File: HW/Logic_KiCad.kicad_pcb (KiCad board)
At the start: 2 copper layers, 100 x 100 mm, 248 parts, among them J1 USB_B_Micro, Q1 Q_NPN_BEC, Q2 Q_NPN_BEC, Q4 Q_NMOS_SDG, Q5 Q_PMOS_SDG, Q6 Q_NMOS_SDG, Q7 Q_PMOS_SDG, Q8 Q_NMOS_SDG, Q9 Q_PMOS_SDG, SW1 SW_SPDT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

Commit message: routing PCB
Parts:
- moved D7 2.34 mm to (107.0, 48.5)
- moved D8 1.84 mm to (107.0, 50.6)
- moved C22 1.57 mm to (107.0, 66.4)
- moved C23 1.56 mm to (105.9, 66.4)
- moved Q1 0.62 mm to (98.4, 72.5)
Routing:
- net GND: track 0.00 -> 515.8 mm, vias 0 -> 119
- net V_LED_1: track 0.00 -> 300.2 mm, vias 0 -> 37
- net V_LED_3: track 0.00 -> 205.2 mm, vias 0 -> 25
- net V_LED_2: track 0.00 -> 197.8 mm, vias 0 -> 25
- net BTN_ENTER: track 0.00 -> 119.6 mm, vias 0 -> 2
- net BTN_NEW_GAME: track 0.00 -> 97.0 mm, vias 0 -> 2
- net BARVA_5: track 0.00 -> 92.9 mm, vias 0 -> 2
- net DATA_hodnoceni_LED: track 0.00 -> 88.8 mm, vias 0 -> 2
- net BARVA_4: track 0.00 -> 88.8 mm, vias 0 -> 2
- net +5V: track 0.00 -> 87.1 mm, vias 0 -> 4
- net BARVA_6: track 0.00 -> 82.6 mm, vias 0 -> 2
- net ZAPINANI_1_CAST_LED: track 0.00 -> 72.0 mm, vias 0 -> 2
- net BARVA_3: track 0.00 -> 61.2 mm
- net DATA_herni_LED: track 0.00 -> 56.6 mm, vias 0 -> 2
- net DATA_zadani_LED: track 0.00 -> 56.5 mm, vias 0 -> 2
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- added copper zone on In1.Cu, net +3V3
- added copper zone on In1.Cu, net +5V
- added copper zone on In2.Cu, net GND
- added copper zone on In1.Cu, net V_LED_1
- added copper zone on In1.Cu, net V_LED_2
- added copper zone on In1.Cu, net V_LED_3
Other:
- copper layers 2 -> 4

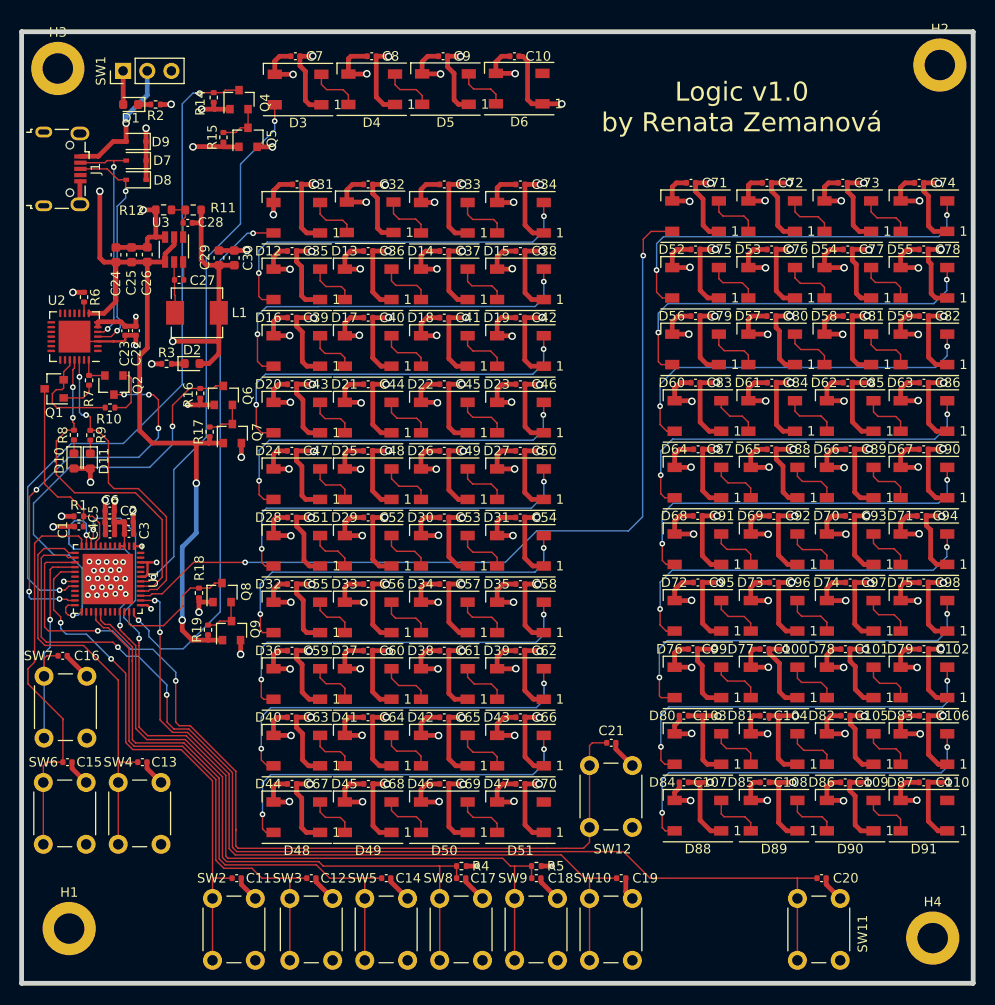
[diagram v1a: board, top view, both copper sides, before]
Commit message: add rounded corners PCB, place mounting holes
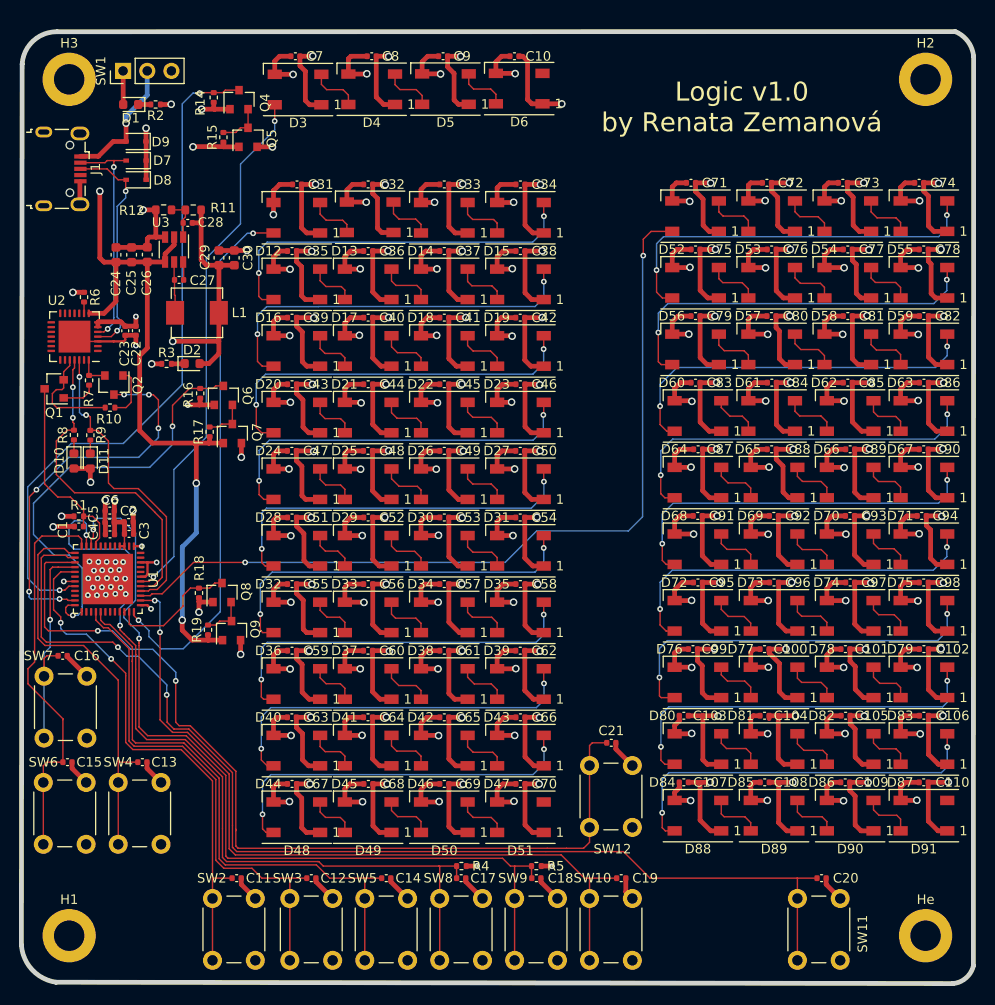
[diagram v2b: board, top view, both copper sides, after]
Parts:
- moved H2 2.12 mm to (190.0, 40.0)
- moved H3 1.65 mm to (100.0, 40.0)
- moved He 0.79 mm to (190.0, 130.0)
- moved H1 0.75 mm to (100.0, 130.0)
- renumbered H4 to He
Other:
- board size 100 x 100 mm -> 100.1 x 100 mm
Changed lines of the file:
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@@
   (general
     (thickness 1.6)
-    (drawings 6)
+    (drawings 10)
     (tracks 2381)
     (zones 0)
@@
     (mod_text_size 1 1)
     (mod_text_width 0.15)
-    (pad_size 1.524 1.524)
-    (pad_drill 0.762)
+    (pad_size 5.6 5.6)
+    (pad_drill 3.2)
     (pad_to_mask_clearance 0.05)
     (aux_axis_origin 0 0)
@@
   )
   (module MountingHole:MountingHole_3.2mm_M3_DIN965_Pad (layer F.Cu)
-    (at 190.75 130.25)
+    (at 190 130)
     (descr "Mounting Hole 3.2mm, M3, DIN965")
     (tags "mounting hole 3.2mm m3 din965")
     (attr virtual)
-    (fp_text reference H4 (at 0 -3.8) (layer F.SilkS)
+    (fp_text reference He (at 0 -3.8) (layer F.SilkS)
       (effects (font (size 1 1) (thickness 0.15)))
     )
@@
   )
   (module MountingHole:MountingHole_3.2mm_M3_DIN965_Pad (layer F.Cu)
-    (at 98.806 38.862)
+    (at 100 40)
     (descr "Mounting Hole 3.2mm, M3, DIN965")
     (tags "mounting hole 3.2mm m3 din965")
@@
   )
   (module MountingHole:MountingHole_3.2mm_M3_DIN965_Pad (layer F.Cu)
-    (at 191.5 38.5)
+    (at 190 40)
     (descr "Mounting Hole 3.2mm, M3, DIN965")
     (tags "mounting hole 3.2mm m3 din965")
@@
   )
   (module MountingHole:MountingHole_3.2mm_M3_DIN965_Pad (layer F.Cu)
-    (at 100 129.25)
+    (at 100 130)
     (descr "Mounting Hole 3.2mm, M3, DIN965")
     (tags "mounting hole 3.2mm m3 din965")
@@
     )
   )
+  (gr_arc (start 99.22 130.68) (end 94.98 131) (angle -77.43958348) (layer Edge.Cuts) (width 0.5))
+  (gr_arc (start 192.64 132.59) (end 192.899999 135.029999) (angle -70.2282783) (layer Edge.Cuts) (width 0.5))
+  (gr_arc (start 191.92 37.89) (end 195.049999 37.590001) (angle -62.01880428) (layer Edge.Cuts) (width 0.5))
+  (gr_arc (start 98.68 38.63) (end 98.729999 35.000001) (angle -87.27940357) (layer Edge.Cuts) (width 0.5))
+  (gr_line (start 98.729999 35.000001) (end 193.123609 34.985139) (layer Edge.Cuts) (width 0.5))
   (gr_text "Logic v1.0\nby Renata Zemanová" (at 170.688 42.926) (layer F.SilkS)
     (effects (font (size 2 2) (thickness 0.15)))
@@
     (effects (font (size 2 2) (thickness 0.15)) (justify mirror))
   )
-  (gr_line (start 95 135) (end 95 35) (layer Edge.Cuts) (width 0.5))
-  (gr_line (start 195 135) (end 95 135) (layer Edge.Cuts) (width 0.5))
-  (gr_line (start 195 35) (end 195 135) (layer Edge.Cuts) (width 0.5))
-  (gr_line (start 95 35) (end 195 35) (layer Edge.Cuts) (width 0.5))
+  (gr_line (start 94.98 131) (end 95.056466 38.407758) (layer Edge.Cuts) (width 0.5))
+  (gr_line (start 192.9 135.03) (end 98.610273 134.888115) (layer Edge.Cuts) (width 0.5))
+  (gr_line (start 195.05 37.59) (end 195.024107 133.170716) (layer Edge.Cuts) (width 0.5))
   (segment (start 101.498 85.946) (end 101.518 85.926) (width 0.15) (layer F.Cu) (net 1))
   (segment (start 101.498 86.996) (end 101.498 85.946) (width 0.15) (layer F.Cu) (net 1))
@@
   (via (at 149.83 75.27) (size 0.6) (drill 0.3) (layers F.Cu B.Cu) (net 49))
   (segment (start 149.872 75.228) (end 149.83 75.27) (width 0.15) (layer F.Cu) (net 49))
-  (segment (start 149.872 73.948) (end 149.872 75.228) (width 0.15) (layer F.Cu) (net 49))
   (segment (start 149.83 75.27) (end 149.83 76.85) (width 0.15) (layer B.Cu) (net 49))
   (segment (start 149.83 76.85) (end 148.75 77.93) (width 0.15) (layer B.Cu) (net 49))
@@
   (segment (start 120.458 84.148) (end 121.472 84.148) (width 0.15) (layer F.Cu) (net 49))
   (segment (start 119.96 83.65) (end 120.458 84.148) (width 0.15) (layer F.Cu) (net 49))
+  (segment (start 149.872 73.948) (end 149.872 75.228) (width 0.15) (layer F.Cu) (net 49))
   (segment (start 128.972 84.148) (end 128.972 83.082) (width 0.15) (layer F.Cu) (net 50))
   (segment (start 128.972 83.082) (end 128.52 82.63) (width 0.15) (layer F.Cu) (net 50))
@@
   (segment (start 108.48399 93.61601) (end 108.33 93.77) (width 0.15) (layer F.Cu) (net 130))
   (segment (start 108.33 93.77) (end 107.912 93.77) (width 0.15) (layer F.Cu) (net 130))
-  (zone (net 2) (net_name GND) (layer In2.Cu) (hatch edge 0.508)
-    (connect_pads (clearance 0.508))
-    (min_thickness 0.254)
-    (fill yes (arc_segments 32) (thermal_gap 0.508) (thermal_bridge_width 0.508))
-    (polygon
-      (pts
-        (xy 195 135) (xy 95 135) (xy 95 35) (xy 195 35)
-      )
-    )
-  )
   (zone (net 4) (net_name V_LED_1) (layer In1.Cu) (hatch edge 0.508)
     (connect_pads (clearance 0.508))
@@
       )
     )
+  )
+  (zone (net 2) (net_name GND) (layer In2.Cu) (hatch edge 0.508)
+    (connect_pads (clearance 0.508))
+    (min_thickness 0.254)
+    (fill yes (arc_segments 32) (thermal_gap 0.508) (thermal_bridge_width 0.508))
+    (polygon
+      (pts
+        (xy 194.88 134) (xy 94.88 134) (xy 94.88 34) (xy 194.88 34)
+      )
+    )

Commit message: repair footprint of P and N MOS, add order codes for JLCPCB, preparing for fab
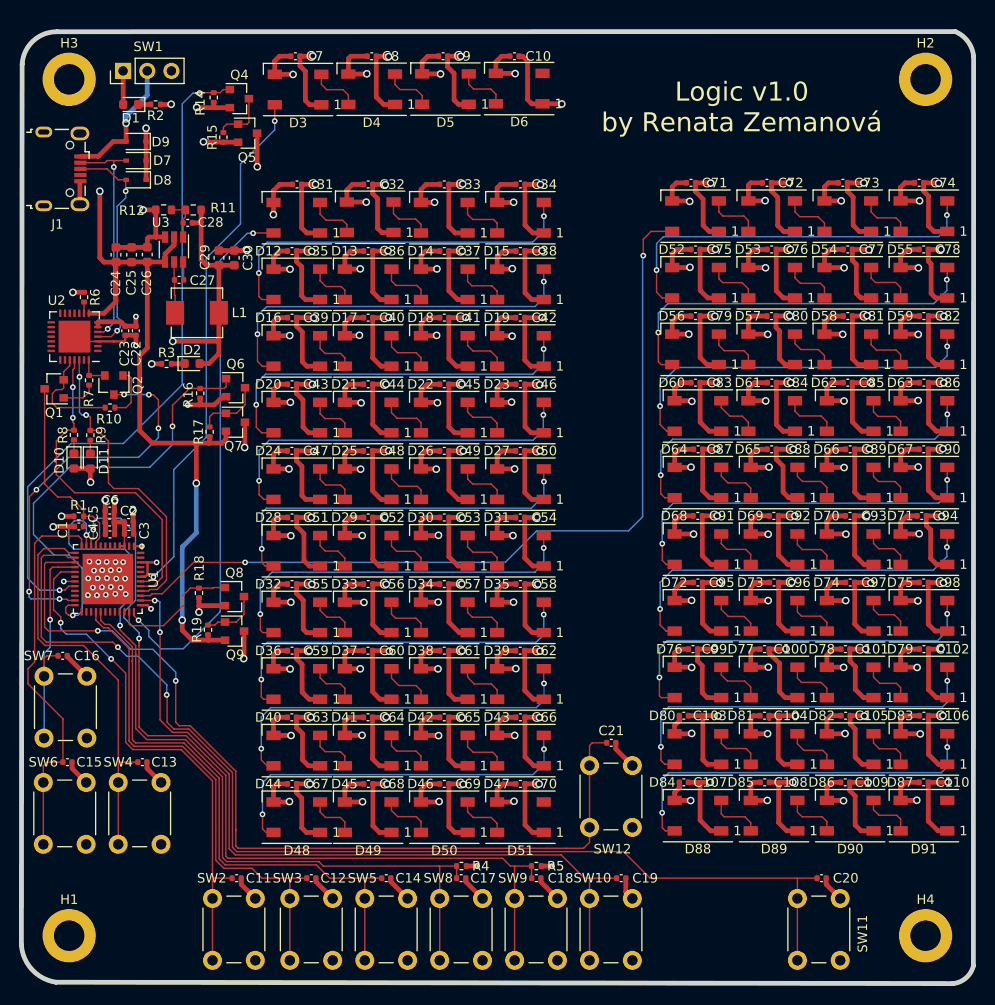
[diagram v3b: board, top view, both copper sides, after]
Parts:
- Q4, Q6, Q8: value Q_NMOS_SDG -> Q_NMOS_GSD
- Q5, Q7, Q9: value Q_PMOS_SDG -> Q_PMOS_GSD
- moved Q6 1.52 mm to (117.5, 72.4), turned to 0 degrees
- moved Q8 1.37 mm to (117.4, 94.4), turned to 0 degrees
- moved Q7 1.23 mm to (117.5, 76.0), turned to 0 degrees
- moved Q5 0.44 mm to (118.8, 45.7), turned to 0 degrees
- moved Q9 0.32 mm to (117.4, 98.0), turned to 0 degrees
- moved Q4 0.12 mm to (117.9, 42.0), turned to 0 degrees
- renumbered He to H4
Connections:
- Q4 pad 1: GND -> ZAPINANI_1_CAST_LED
- Q4 pad 2: Net-(Q4-Pad2) -> GND
- Q4 pad 3: ZAPINANI_1_CAST_LED -> Net-(Q4-Pad3)
- Q5 pad 1: +5V -> Net-(Q4-Pad3)
- Q5 pad 2: V_LED_1 -> +5V
- Q5 pad 3: Net-(Q4-Pad2) -> V_LED_1
- Q6 pad 1: GND -> ZAPINANI_2_CAST_LED
- Q6 pad 2: Net-(Q6-Pad2) -> GND
- Q6 pad 3: ZAPINANI_2_CAST_LED -> Net-(Q6-Pad3)
- Q7 pad 1: +5V -> Net-(Q6-Pad3)
- Q7 pad 2: V_LED_2 -> +5V
- Q7 pad 3: Net-(Q6-Pad2) -> V_LED_2
- Q8 pad 1: GND -> ZAPINANI_3_CAST_LED
- Q8 pad 2: Net-(Q8-Pad2) -> GND
- Q8 pad 3: ZAPINANI_3_CAST_LED -> Net-(Q8-Pad3)
- Q9 pad 1: +5V -> Net-(Q8-Pad3)
- Q9 pad 2: V_LED_3 -> +5V
- Q9 pad 3: Net-(Q8-Pad2) -> V_LED_3
- R15 pad 2: Net-(Q4-Pad2) -> Net-(Q4-Pad3)
- R17 pad 2: Net-(Q6-Pad2) -> Net-(Q6-Pad3)
- R19 pad 2: Net-(Q8-Pad2) -> Net-(Q8-Pad3)
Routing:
- net Net-(Q6-Pad3): track 0.00 -> 7.13 mm
- net Net-(Q8-Pad3): track 0.00 -> 6.11 mm
- net Net-(Q4-Pad3): track 0.00 -> 5.94 mm
- net Net-(Q4-Pad2): track 4.75 -> 0.00 mm
- net Net-(Q8-Pad2): track 4.67 -> 0.00 mm
- net Net-(Q6-Pad2): track 4.53 -> 0.00 mm
- net GND: track 515.8 -> 519.0 mm
- net V_LED_1: track 300.2 -> 302.1 mm
- net V_LED_3: track 205.2 -> 206.6 mm
- net V_LED_2: track 197.8 -> 198.9 mm
- net ZAPINANI_2_CAST_LED: track 45.5 -> 46.6 mm
- net ZAPINANI_1_CAST_LED: track 72.0 -> 71.1 mm

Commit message: nicer routing
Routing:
- net DATA_hodnoceni_LED: track 88.8 -> 83.7 mm
- net BTN_ENTER: track 119.6 -> 115.3 mm
- net BARVA_3: track 61.2 -> 56.9 mm
- net BARVA_1: track 55.8 -> 51.6 mm
- net BARVA_2: track 53.6 -> 49.4 mm
- net BTN_NEW_GAME: track 97.0 -> 93.2 mm
- net BARVA_5: track 92.9 -> 89.3 mm
- net BARVA_4: track 88.8 -> 85.4 mm
- net ZAPINANI_2_CAST_LED: track 46.6 -> 44.6 mm
- net BARVA_6: track 82.6 -> 80.9 mm
- net BTN_SIPKA_VPRAVO: track 42.7 -> 41.4 mm
- net EN: track 21.5 -> 20.7 mm

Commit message: repair mistakes
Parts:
- C22: value 4u7 -> 10u
- R15, R17, R19: value 10k -> 100k
- R6: value 2k -> 10k
- R8, R9: value 47k -> 10k
- moved C5 10.8 mm to (109.3, 96.0), turned to 180 degrees
- moved C6 9.47 mm to (98.8, 93.1), turned to 90 degrees
- moved D1 7.06 mm to (112.7, 46.0), turned to 90 degrees
- moved R2 6.98 mm to (112.7, 48.6), turned to 90 degrees
- moved C3 5.16 mm to (109.2, 92.0)
- moved C2 4.53 mm to (108.8, 90.3), turned to 90 degrees
- moved SW1 3.85 mm to (109.2, 37.6)
- moved J1 3.41 mm to (99.3, 52.8)
- moved D7 2.01 mm to (107.0, 50.5)
- moved D8 2.00 mm to (107.0, 48.6)
- moved R18 1.24 mm to (114.9, 93.9)
- moved R17 0.68 mm to (115.1, 76.5)
- moved R19 0.67 mm to (114.9, 98.4)
- moved R8 0.56 mm to (100.0, 77.3)
- moved C4 0.53 mm to (104.8, 87.8)
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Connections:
- J1 pad 6: GND -> Net-(J1-Pad6)
- R8 pad 2: TX_ESP -> Net-(R8-Pad2)
- R9 pad 2: RX_ESP -> Net-(R9-Pad2)
- U2 pad 18: Net-(U2-Pad18) -> Net-(R9-Pad2)
- U2 pad 19: Net-(U2-Pad19) -> Net-(R8-Pad2)
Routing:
- net +5V: track 86.9 -> 29.2 mm, vias 4 -> 5
- net Net-(R9-Pad2): track 0.00 -> 18.4 mm, vias 0 -> 2
- net Net-(J1-Pad6): track 0.00 -> 15.5 mm
- net Net-(R8-Pad2): track 0.00 -> 13.2 mm, vias 0 -> 2
- net DATA_hodnoceni_LED: track 83.7 -> 91.7 mm, vias 2 -> 0
- net V_IN: track 13.8 -> 21.3 mm, vias 1 -> 0
- net Net-(D8-Pad2): track 23.8 -> 30.2 mm, vias 2 -> 4
- net RX_ESP: track 32.1 -> 35.7 mm
- net TX_ESP: track 35.1 -> 38.5 mm
- net BTN_END: track 23.9 -> 26.1 mm
- net BARVA_1: track 51.6 -> 53.6 mm
- net BTN_NEW_GAME: track 93.2 -> 94.7 mm
- net BTN_ENTER: track 115.3 -> 116.8 mm
- net +3V3: track 55.1 -> 56.4 mm, vias 12 -> 11
- net GND: track 519.2 -> 518.0 mm, vias 119 -> 123
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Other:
- board text added: "Fialová"
- board text added: "Konec"
- board text added: "Modrá"
- board text added: "Nová hra"
- board text added: "Oranžová"
- board text added: "Potvrdit tah"
- board text added: "Zelená"
- board text added: "Červená"
- board text added: "Šipka vlevo"
- board text added: "Šipka vpravo"
- board text added: "Žlutá"

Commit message: v1.0 for fab
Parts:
- moved D8 2.12 mm to (107.0, 50.7)
- moved D7 1.93 mm to (107.0, 48.6)
- moved R16 1.37 mm to (115.1, 72.8)
- moved C22 0.34 mm to (106.7, 66.4)
- moved C23 0.26 mm to (105.6, 66.4)
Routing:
- net +3V3: track 56.4 -> 69.1 mm
- net Net-(D8-Pad2): track 30.2 -> 24.7 mm, vias 4 -> 2
- net Net-(D7-Pad2): track 23.9 -> 28.6 mm
- net GND: track 518.0 -> 514.4 mm, vias 123 -> 122
- net V_IN: track 21.3 -> 19.5 mm
- net /herni_LED.sch/8.sch/DATA_IN: track 40.2 -> 38.8 mm
- net V_LED_3: track 206.6 -> 207.4 mm
- net V_LED_1: track 302.1 -> 301.3 mm
- net ZAPINANI_2_CAST_LED: track 43.8 -> 43.2 mm
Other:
- board size 100.1 x 100 mm -> 100 x 100 mm
- board text added: "Power 3V3"
- board text added: "Power 5V"
